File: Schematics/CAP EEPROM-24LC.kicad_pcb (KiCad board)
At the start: 2 copper layers, 49.5 x 30.5 mm, 7 parts, among them IC1 24LC128, K1 CAP_CONN_LHS, K2 CAP_CONN_RHS, P1 A2_SEL

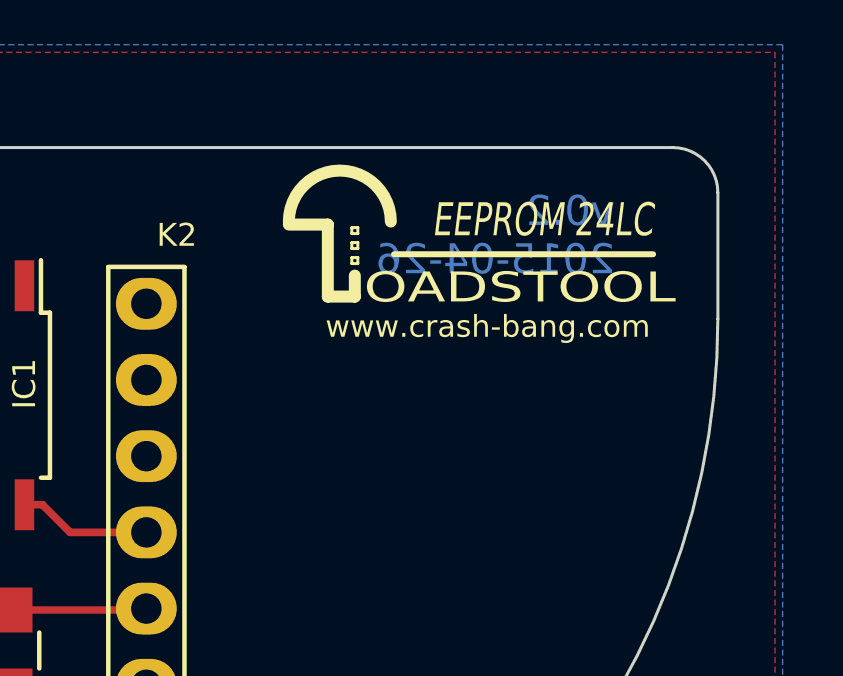
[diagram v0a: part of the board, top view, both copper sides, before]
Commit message: Cosmetic Changes to Silkscreen
Cosmetic Changes to Silkscreen
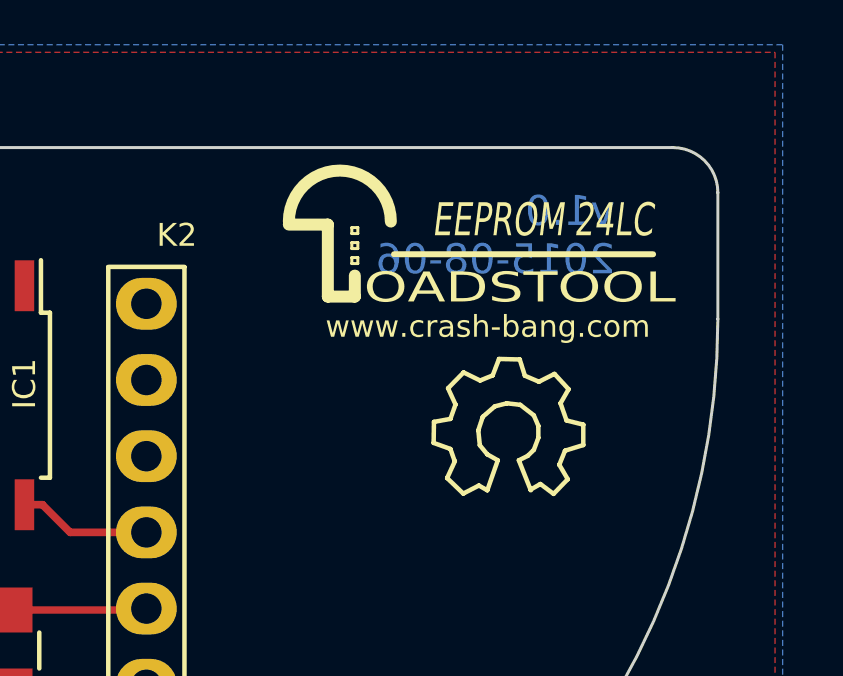
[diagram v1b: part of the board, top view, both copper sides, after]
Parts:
- added REF**: Symbol_OSHW-Logo_SilkScreen, Toadstool:Symbol_OSHW-Logo_SilkScreen, F.Cu at (226.1, 108.0)
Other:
- board text added: "v1.0 2015-08-06"
- board text removed: "v0.2 2015-04-26"
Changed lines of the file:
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@@
     (links 14)
     (no_connects 0)
-    (area 183.464999 98.374999 233.095001 128.955001)
+    (area 180.594 94.996 244.065097 132.842001)
     (thickness 1.6)
     (drawings 14)
     (tracks 23)
     (zones 0)
-    (modules 7)
+    (modules 8)
     (nets 14)
   )
@@
     )
   )
+  (module Toadstool:Symbol_OSHW-Logo_SilkScreen (layer F.Cu)
+    (at 226.06 107.95)
+    (descr "Symbol, OSHW-Logo, Silk Screen,")
+    (tags "Symbol, OSHW-Logo, Silk Screen,")
+    (fp_text reference REF** (at -0.127 -3.302) (layer F.SilkS) hide
+      (effects (font (size 1 1) (thickness 0.15)))
+    )
+    (fp_text value Symbol_OSHW-Logo_SilkScreen (at 0 3.175) (layer F.Fab) hide
+      (effects (font (size 1 1) (thickness 0.15)))
+    )
+    (fp_line (start -1.78054 0.92964) (end -2.03962 1.49098) (layer F.SilkS) (width 0.15))
+    (fp_line (start -2.03962 1.49098) (end -1.50114 2.00914) (layer F.SilkS) (width 0.15))
+    (fp_line (start -1.50114 2.00914) (end -0.98044 1.7399) (layer F.SilkS) (width 0.15))
+    (fp_line (start -0.98044 1.7399) (end -0.70104 1.89992) (layer F.SilkS) (width 0.15))
+    (fp_line (start 0.73914 1.8796) (end 1.06934 1.6891) (layer F.SilkS) (width 0.15))
+    (fp_line (start 1.06934 1.6891) (end 1.50876 2.0193) (layer F.SilkS) (width 0.15))
+    (fp_line (start 1.50876 2.0193) (end 1.9812 1.52908) (layer F.SilkS) (width 0.15))
+    (fp_line (start 1.9812 1.52908) (end 1.69926 1.04902) (layer F.SilkS) (width 0.15))
+    (fp_line (start 1.69926 1.04902) (end 1.88976 0.57912) (layer F.SilkS) (width 0.15))
+    (fp_line (start 1.88976 0.57912) (end 2.49936 0.39116) (layer F.SilkS) (width 0.15))
+    (fp_line (start 2.49936 0.39116) (end 2.49936 -0.28956) (layer F.SilkS) (width 0.15))
+    (fp_line (start 2.49936 -0.28956) (end 1.94056 -0.42926) (layer F.SilkS) (width 0.15))
+    (fp_line (start 1.94056 -0.42926) (end 1.7399 -1.00076) (layer F.SilkS) (width 0.15))
+    (fp_line (start 1.7399 -1.00076) (end 2.00914 -1.47066) (layer F.SilkS) (width 0.15))
+    (fp_line (start 2.00914 -1.47066) (end 1.53924 -1.9812) (layer F.SilkS) (width 0.15))
+    (fp_line (start 1.53924 -1.9812) (end 1.02108 -1.71958) (layer F.SilkS) (width 0.15))
+    (fp_line (start 1.02108 -1.71958) (end 0.55118 -1.92024) (layer F.SilkS) (width 0.15))
+    (fp_line (start 0.55118 -1.92024) (end 0.381 -2.46126) (layer F.SilkS) (width 0.15))
+    (fp_line (start 0.381 -2.46126) (end -0.30988 -2.47904) (layer F.SilkS) (width 0.15))
+    (fp_line (start -0.30988 -2.47904) (end -0.5207 -1.9304) (layer F.SilkS) (width 0.15))
+    (fp_line (start -0.5207 -1.9304) (end -0.9398 -1.76022) (layer F.SilkS) (width 0.15))
+    (fp_line (start -0.9398 -1.76022) (end -1.49098 -2.02946) (layer F.SilkS) (width 0.15))
+    (fp_line (start -1.49098 -2.02946) (end -2.00914 -1.50114) (layer F.SilkS) (width 0.15))
+    (fp_line (start -2.00914 -1.50114) (end -1.76022 -0.96012) (layer F.SilkS) (width 0.15))
+    (fp_line (start -1.76022 -0.96012) (end -1.9304 -0.48006) (layer F.SilkS) (width 0.15))
+    (fp_line (start -1.9304 -0.48006) (end -2.47904 -0.381) (layer F.SilkS) (width 0.15))
+    (fp_line (start -2.47904 -0.381) (end -2.4892 0.32004) (layer F.SilkS) (width 0.15))
+    (fp_line (start -2.4892 0.32004) (end -1.9304 0.5207) (layer F.SilkS) (width 0.15))
+    (fp_line (start -1.9304 0.5207) (end -1.7907 0.91948) (layer F.SilkS) (width 0.15))
+    (fp_line (start 0.35052 0.89916) (end 0.65024 0.7493) (layer F.SilkS) (width 0.15))
+    (fp_line (start 0.65024 0.7493) (end 0.8509 0.55118) (layer F.SilkS) (width 0.15))
+    (fp_line (start 0.8509 0.55118) (end 1.00076 0.14986) (layer F.SilkS) (width 0.15))
+    (fp_line (start 1.00076 0.14986) (end 1.00076 -0.24892) (layer F.SilkS) (width 0.15))
+    (fp_line (start 1.00076 -0.24892) (end 0.8509 -0.59944) (layer F.SilkS) (width 0.15))
+    (fp_line (start 0.8509 -0.59944) (end 0.39878 -0.94996) (layer F.SilkS) (width 0.15))
+    (fp_line (start 0.39878 -0.94996) (end -0.0508 -1.00076) (layer F.SilkS) (width 0.15))
+    (fp_line (start -0.0508 -1.00076) (end -0.44958 -0.89916) (layer F.SilkS) (width 0.15))
+    (fp_line (start -0.44958 -0.89916) (end -0.8509 -0.55118) (layer F.SilkS) (width 0.15))
+    (fp_line (start -0.8509 -0.55118) (end -1.00076 -0.09906) (layer F.SilkS) (width 0.15))
+    (fp_line (start -1.00076 -0.09906) (end -0.94996 0.39878) (layer F.SilkS) (width 0.15))
+    (fp_line (start -0.94996 0.39878) (end -0.70104 0.70104) (layer F.SilkS) (width 0.15))
+    (fp_line (start -0.70104 0.70104) (end -0.35052 0.89916) (layer F.SilkS) (width 0.15))
+    (fp_line (start -0.35052 0.89916) (end -0.70104 1.89992) (layer F.SilkS) (width 0.15))
+    (fp_line (start 0.35052 0.89916) (end 0.7493 1.89992) (layer F.SilkS) (width 0.15))
+  )
   (gr_text "I2C Address:\n1010[A2]11" (at 216.535 122.301) (layer F.SilkS)
     (effects (font (size 0.762 0.762) (thickness 0.1905)))
@@
   (gr_arc (start 231.545 99.925) (end 231.545 98.425) (angle 90) (layer Edge.Cuts) (width 0.1))
   (gr_arc (start 185.015 99.925) (end 183.515 99.925) (angle 90) (layer Edge.Cuts) (width 0.1))
-  (gr_text "v0.2\n2015-04-26" (at 229.616 101.346) (layer B.Cu)
+  (gr_text "v1.0\n2015-08-06" (at 229.616 101.346) (layer B.Cu)
     (effects (font (size 1 1) (thickness 0.2)) (justify left mirror))
   )
@@
   (gr_arc (start 208.28 104.14) (end 233.045 104.14) (angle 180) (layer Edge.Cuts) (width 0.1))
   (gr_line (start 231.545 98.425) (end 185.015 98.425) (angle 90) (layer Edge.Cuts) (width 0.1))
+  (segment (start 208.661 109.22) (end 208.026 108.585) (width 0.254) (layer F.Cu) (net 1))
+  (segment (start 208.026 108.585) (end 205.232 108.585) (width 0.254) (layer F.Cu) (net 1))
+  (segment (start 205.232 108.585) (end 202.565 111.252) (width 0.254) (layer F.Cu) (net 1))
+  (segment (start 208.661 110.33) (end 208.661 109.22) (width 0.254) (layer F.Cu) (net 1))
+  (segment (start 206.121 107.696) (end 205.232 108.585) (width 0.254) (layer F.Cu) (net 1))
   (segment (start 206.121 103.03) (end 206.121 107.696) (width 0.254) (layer F.Cu) (net 1))
-  (segment (start 206.121 107.696) (end 205.232 108.585) (width 0.254) (layer F.Cu) (net 1))
-  (segment (start 208.661 110.33) (end 208.661 109.22) (width 0.254) (layer F.Cu) (net 1))
-  (segment (start 205.232 108.585) (end 202.565 111.252) (width 0.254) (layer F.Cu) (net 1))
-  (segment (start 208.026 108.585) (end 205.232 108.585) (width 0.254) (layer F.Cu) (net 1))
-  (segment (start 208.661 109.22) (end 208.026 108.585) (width 0.254) (layer F.Cu) (net 1))
+  (segment (start 210.533 110.33) (end 211.455 111.252) (width 0.254) (layer F.Cu) (net 2))
+  (segment (start 211.455 111.252) (end 213.995 111.252) (width 0.254) (layer F.Cu) (net 2))
   (segment (start 209.931 110.33) (end 210.533 110.33) (width 0.254) (layer F.Cu) (net 2))
-  (segment (start 211.455 111.252) (end 213.995 111.252) (width 0.254) (layer F.Cu) (net 2))
-  (segment (start 210.533 110.33) (end 211.455 111.252) (width 0.254) (layer F.Cu) (net 2))
+  (segment (start 213.948 113.839) (end 213.995 113.792) (width 0.254) (layer F.Cu) (net 3))
+  (segment (start 209.55 113.839) (end 213.948 113.839) (width 0.254) (layer F.Cu) (net 3))
+  (segment (start 207.391 111.76) (end 207.391 110.33) (width 0.254) (layer F.Cu) (net 3))
+  (segment (start 209.47 113.839) (end 207.391 111.76) (width 0.254) (layer F.Cu) (net 3))
   (segment (start 209.55 113.839) (end 209.47 113.839) (width 0.254) (layer F.Cu) (net 3))
-  (segment (start 209.47 113.839) (end 207.391 111.76) (width 0.254) (layer F.Cu) (net 3))
-  (segment (start 207.391 111.76) (end 207.391 110.33) (width 0.254) (layer F.Cu) (net 3))
-  (segment (start 209.55 113.839) (end 213.948 113.839) (width 0.254) (layer F.Cu) (net 3))
-  (segment (start 213.948 113.839) (end 213.995 113.792) (width 0.254) (layer F.Cu) (net 3))
+  (segment (start 202.612 113.839) (end 202.565 113.792) (width 0.254) (layer F.Cu) (net 4))
+  (segment (start 206.629 113.839) (end 202.612 113.839) (width 0.254) (layer F.Cu) (net 4))
+  (segment (start 206.629 112.268) (end 206.121 111.76) (width 0.254) (layer F.Cu) (net 4))
+  (segment (start 206.121 111.76) (end 206.121 110.33) (width 0.254) (layer F.Cu) (net 4))
   (segment (start 206.629 113.839) (end 206.629 112.268) (width 0.254) (layer F.Cu) (net 4))
-  (segment (start 206.121 111.76) (end 206.121 110.33) (width 0.254) (layer F.Cu) (net 4))
-  (segment (start 206.629 112.268) (end 206.121 111.76) (width 0.254) (layer F.Cu) (net 4))
-  (segment (start 206.629 113.839) (end 202.612 113.839) (width 0.254) (layer F.Cu) (net 4))
-  (segment (start 202.612 113.839) (end 202.565 113.792) (width 0.254) (layer F.Cu) (net 4))
+  (via (at 208.153 106.807) (size 0.889) (layers F.Cu B.Cu) (net 5))
+  (segment (start 208.153 106.807) (end 207.391 106.045) (width 0.254) (layer F.Cu) (net 5))
+  (segment (start 207.391 106.045) (end 207.391 103.03) (width 0.254) (layer F.Cu) (net 5))
   (segment (start 208.153 122.174) (end 208.153 106.807) (width 0.254) (layer B.Cu) (net 5))
-  (segment (start 207.391 106.045) (end 207.391 103.03) (width 0.254) (layer F.Cu) (net 5))
-  (segment (start 208.153 106.807) (end 207.391 106.045) (width 0.254) (layer F.Cu) (net 5))
-  (via (at 208.153 106.807) (size 0.889) (layers F.Cu B.Cu) (net 5))
   (zone (net 2) (net_name VCC) (layer F.Cu) (hatch edge 0.508)
     (connect_pads (clearance 0.508))
